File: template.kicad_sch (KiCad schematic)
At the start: 2 parts, among them J1 Screw Terminal Block 5.00 mm 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

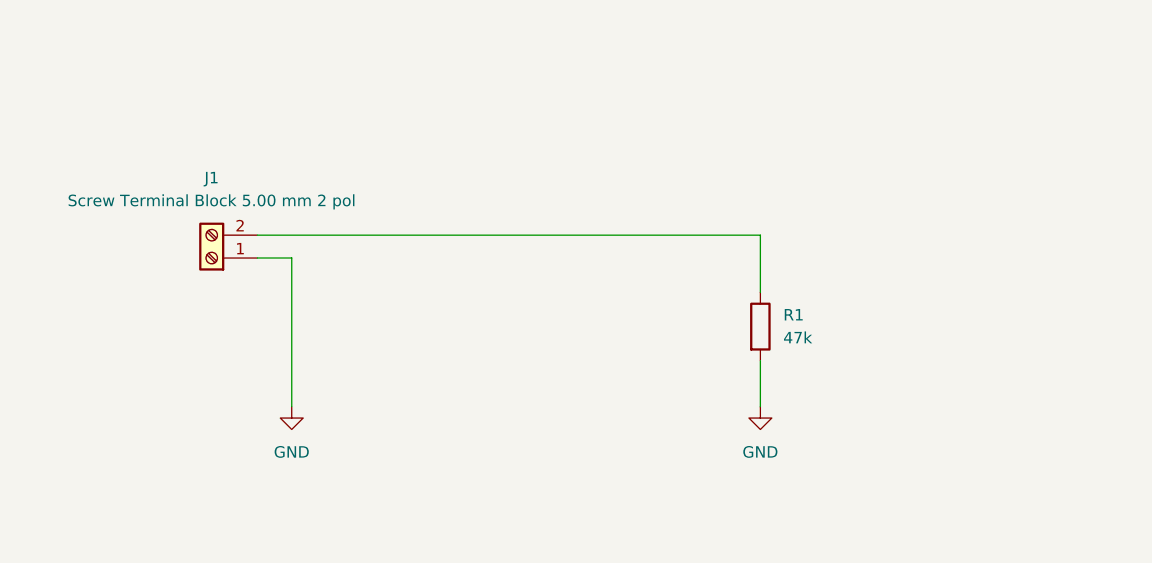
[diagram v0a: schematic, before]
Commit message: feat: add OpenPnP position file export with top/bottom split
Add KiBot position output for pick and place machines (OpenPnP),
generating separate CSV files for top and bottom SMD populated
components. Also add connector_board test design and update template
schematic/PCB with bottom-side components for testing.

Co-Authored-By: Claude Opus 4.6 <noreply@anthropic.com>
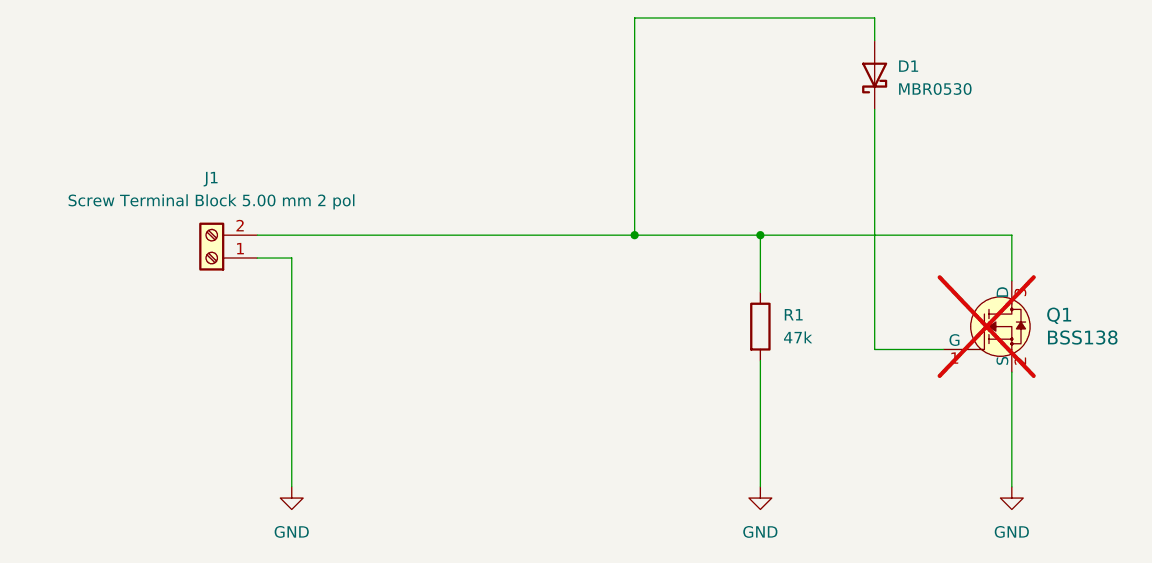
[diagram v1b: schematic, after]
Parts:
- added D1: MBR0530, Diode_SMD:D_SOD-123, symbol 2s_diodes:MBR0530
- added Q1: BSS138, Package_TO_SOT_SMD:SOT-23-3, symbol 2s_transistors:BSS138
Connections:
- net GND: now also Q1.2 (S)
- net at J1.2 (Pin_2), R1.1: now also D1.2 (A), Q1.3 (D)
- new net: D1.1 (K), Q1.1 (G)
